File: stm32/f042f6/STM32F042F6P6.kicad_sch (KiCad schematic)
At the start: 29 parts, among them J1 STLINK, J3 L, J3 USB_C_REC_16PIN, J4 R, SW1 BOOT0, U1 XC6220B331MR, U2 STM32F042F6Px, Y1 8 MHz

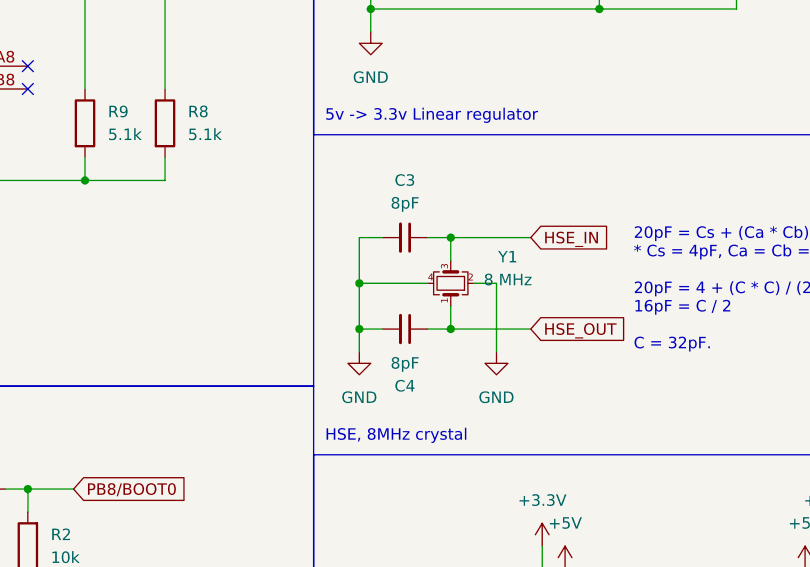
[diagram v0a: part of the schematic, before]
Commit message: Update README.md and mistyped capacitor size correction.
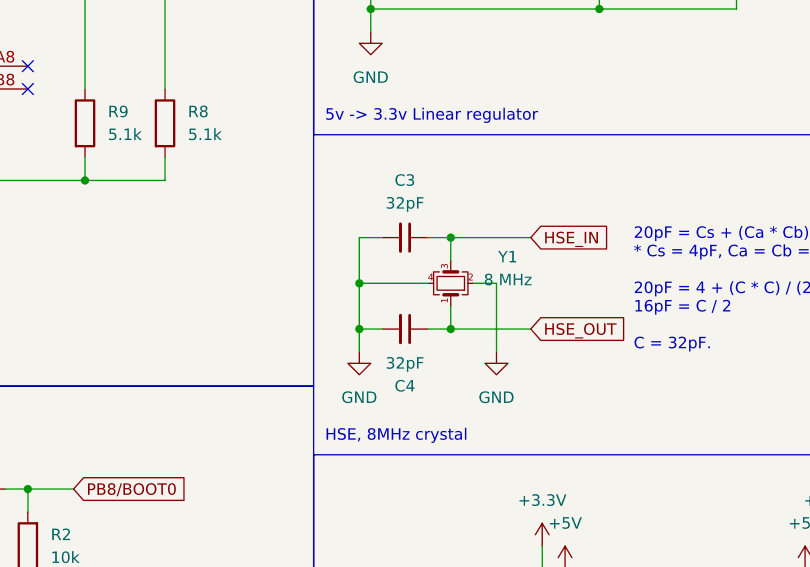
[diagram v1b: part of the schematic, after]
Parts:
- C3, C4: value 8pF -> 32pF
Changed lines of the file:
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@@
       (effects (font (size 1.27 1.27)))
     )
-    (property "Value" "8pF" (at 95.2436 77.47 90)
+    (property "Value" "32pF" (at 95.2436 77.47 90)
       (effects (font (size 1.27 1.27)))
     )
@@
       (effects (font (size 1.27 1.27)))
     )
-    (property "Value" "8pF" (at 95.2436 95.25 90)
-      (effects (font (size 1.27 1.27)))
-    )
+    (property "Value" "32pF" (at 95.2436 95.25 90)
+      (effects (font (size 1.27 1.27)))
+    )

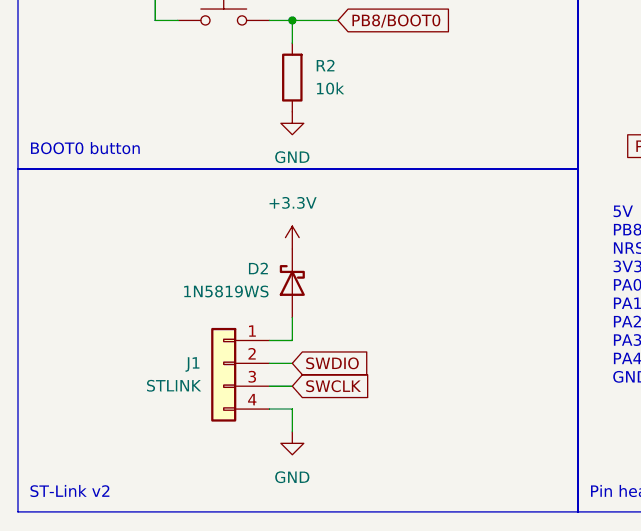
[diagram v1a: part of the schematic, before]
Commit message: WIP: F070F6P6, Fix: Diode direction corrected for F042F6P6.
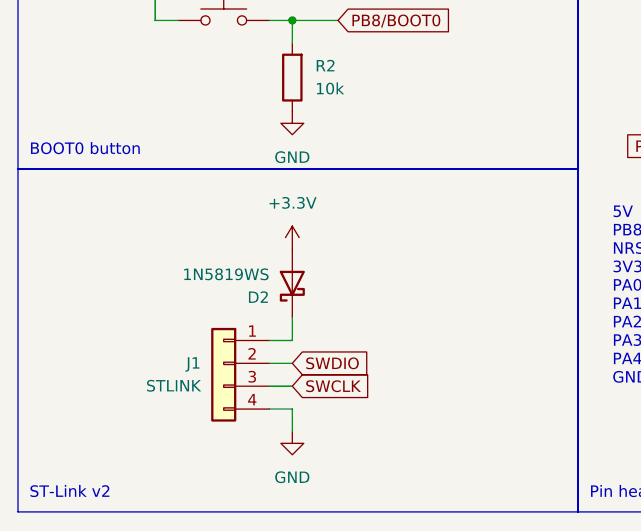
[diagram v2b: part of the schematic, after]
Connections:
- net +3.3V: now also D2.2 (A); no longer D2.1 (K)
- net at J1.1 (Pin_1): now also D2.1 (K); no longer D2.2 (A)
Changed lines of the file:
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@@
     )
   )
-  (symbol (lib_id "Diode:1N5819WS") (at 53.34 138.43 90) (mirror x) (unit 1)
+  (symbol (lib_id "Diode:1N5819WS") (at 53.34 138.43 90) (unit 1)
     (in_bom yes) (on_board yes) (dnp no)
-    (property "Reference" "D2" (at 50.8 136.8425 90)
+    (property "Reference" "D2" (at 50.8 140.0175 90)
       (effects (font (size 1.27 1.27)) (justify left))
     )
-    (property "Value" "1N5819WS" (at 50.8 139.3825 90)
+    (property "Value" "1N5819WS" (at 50.8 137.4775 90)
       (effects (font (size 1.27 1.27)) (justify left))
     )

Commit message: Fix: Diode direction corrected.
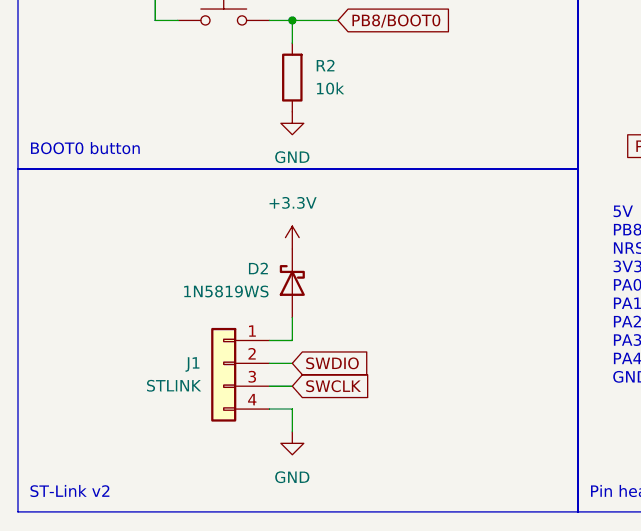
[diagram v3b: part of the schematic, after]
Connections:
- net +3.3V: now also D2.1 (K); no longer D2.2 (A)
- net at J1.1 (Pin_1): now also D2.2 (A); no longer D2.1 (K)
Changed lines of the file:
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@@
     )
   )
-  (symbol (lib_id "Diode:1N5819WS") (at 53.34 138.43 90) (unit 1)
+  (symbol (lib_id "Diode:1N5819WS") (at 53.34 138.43 90) (mirror x) (unit 1)
     (in_bom yes) (on_board yes) (dnp no)
-    (property "Reference" "D2" (at 50.8 140.0175 90)
+    (property "Reference" "D2" (at 50.8 136.8425 90)
       (effects (font (size 1.27 1.27)) (justify left))
     )
-    (property "Value" "1N5819WS" (at 50.8 137.4775 90)
+    (property "Value" "1N5819WS" (at 50.8 139.3825 90)
       (effects (font (size 1.27 1.27)) (justify left))
     )

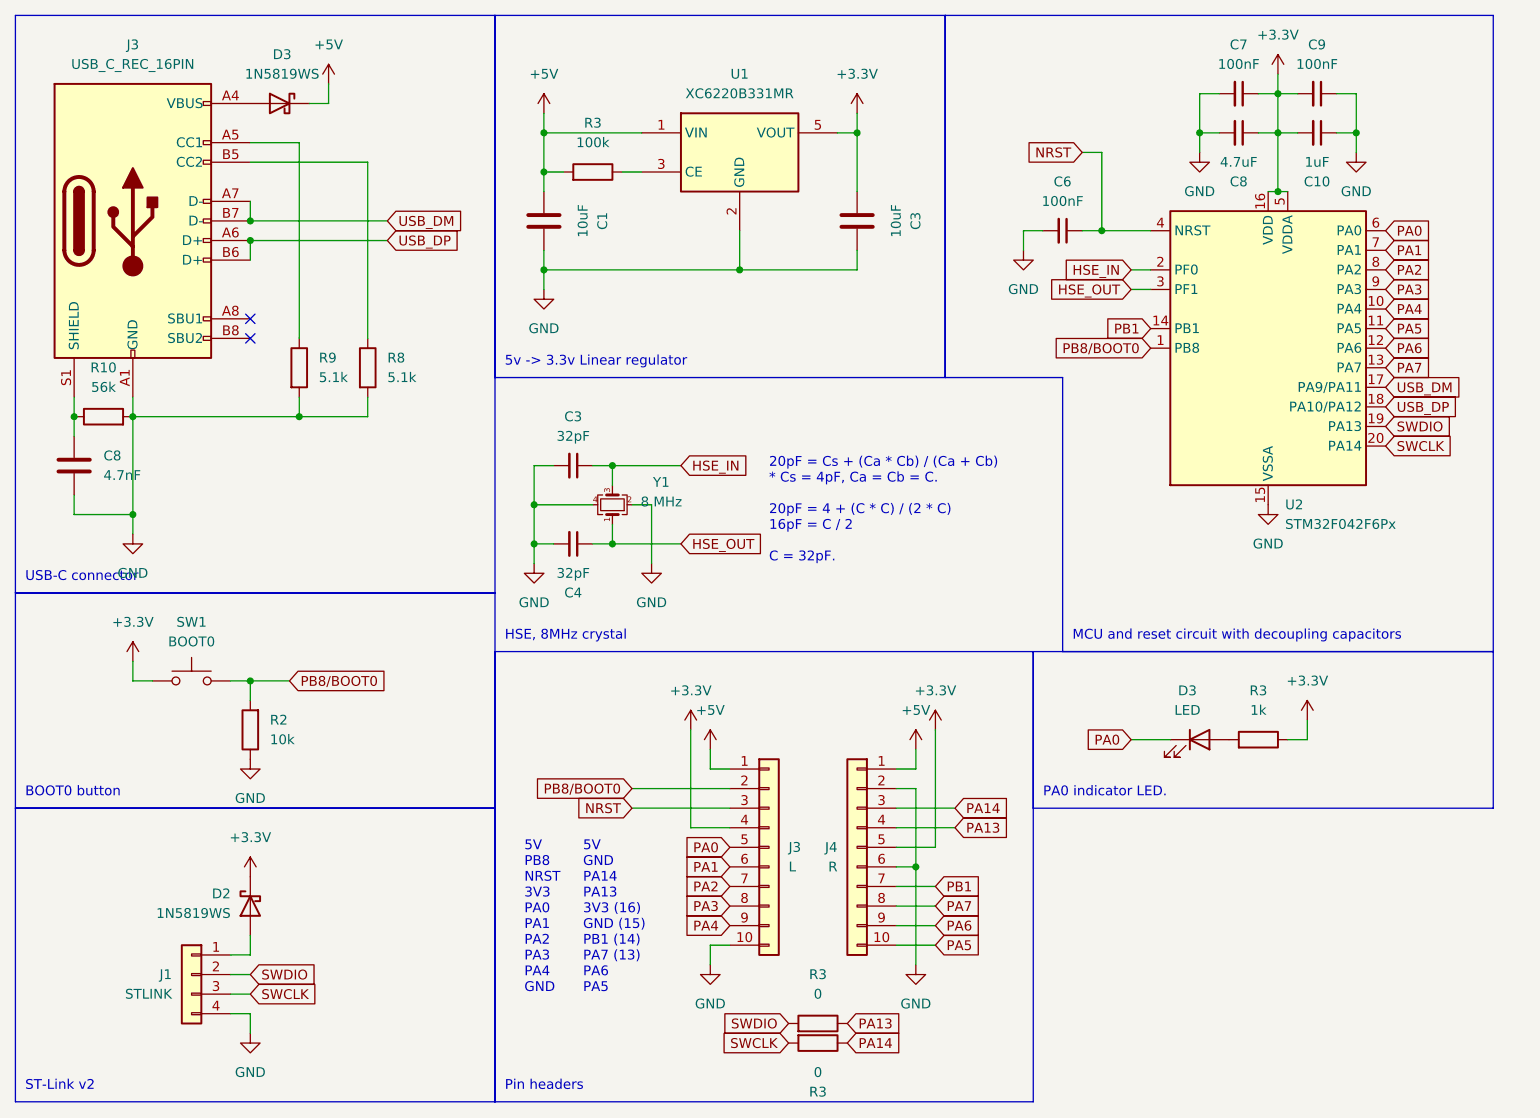
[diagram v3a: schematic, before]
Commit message: F042: HSE crystal removal because it didn't be needed.
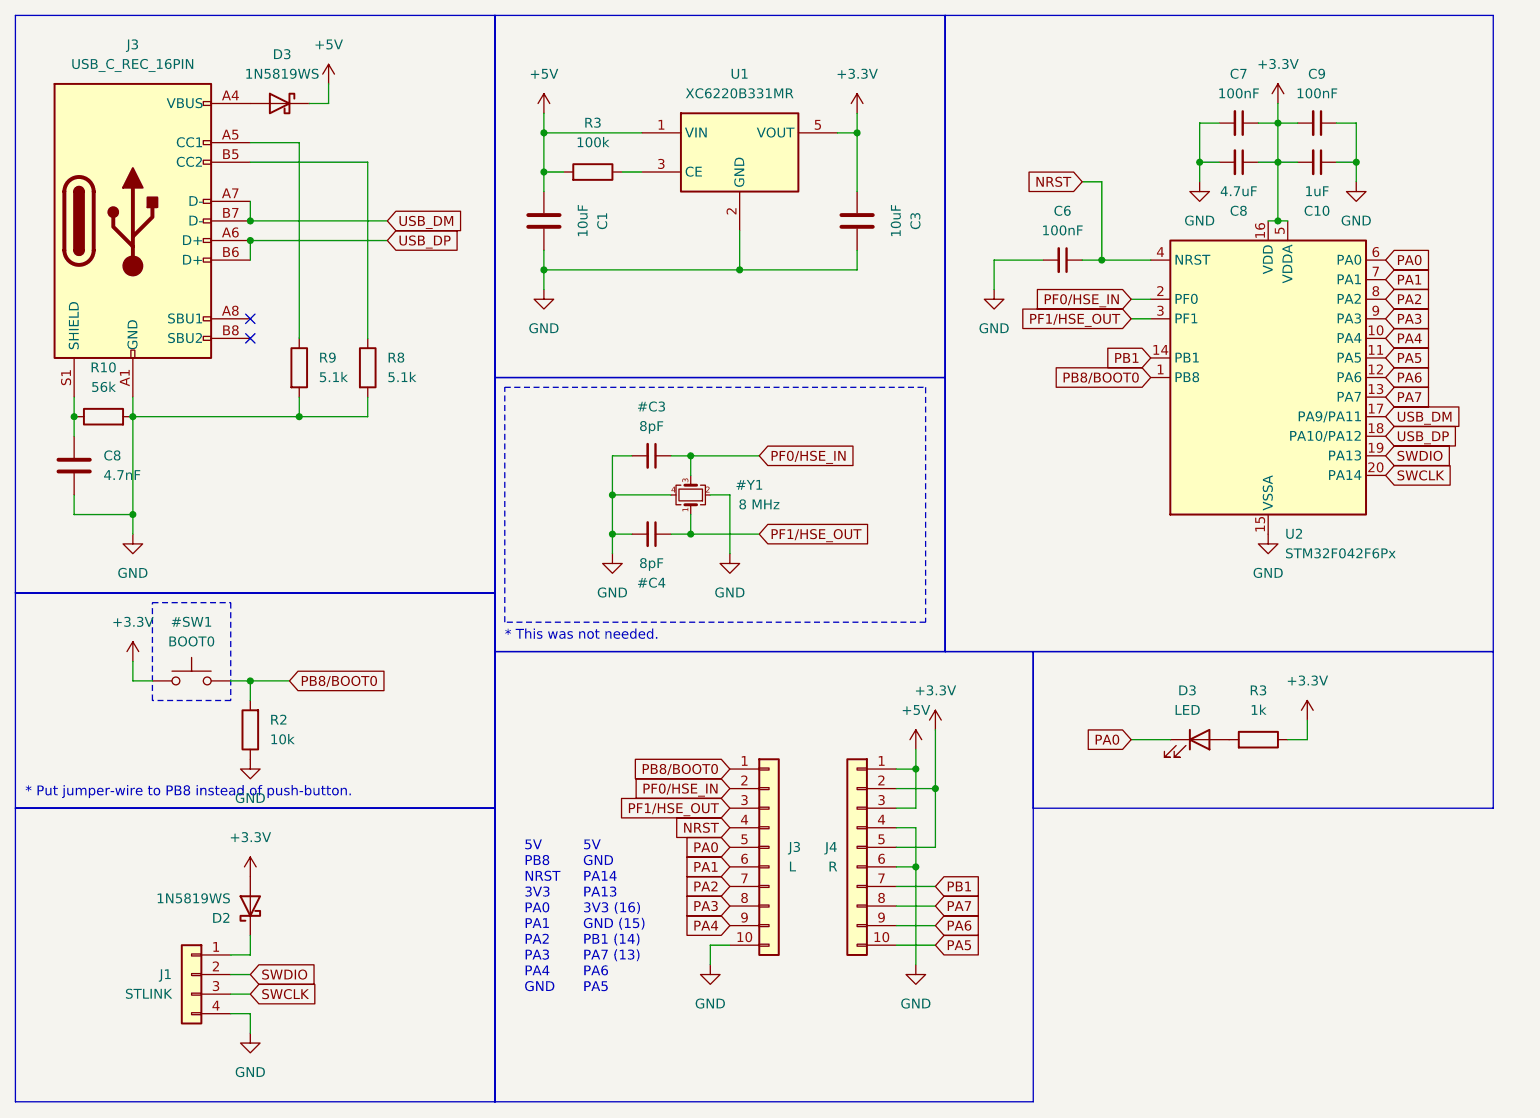
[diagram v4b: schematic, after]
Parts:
- removed R3 (x2): 0, Resistor_SMD:R_0603_1608Metric, symbol Device:R
- #C3: renamed from C3; value 32pF -> 8pF
- #C4: renamed from C4; value 32pF -> 8pF
- renumbered SW1 to #SW1, Y1 to #Y1
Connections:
- net PA13 is gone; now on net GND: J4.4 (Pin_4)
- net PA14 is gone; now on net +5V: J4.3 (Pin_3)
- net +3.3V: now also D2.2 (A), J4.2 (Pin_2); no longer D2.1 (K), J3.4 (Pin_4)
- net +5V: no longer J3.1 (Pin_1)
- net GND: no longer J4.2 (Pin_2)
- net NRST: now also J3.4 (Pin_4); no longer J3.3 (Pin_3)
- net PB8/BOOT0: now also J3.1 (Pin_1); no longer J3.2 (Pin_2)
- net at J1.1 (Pin_1): now also D2.1 (K); no longer D2.2 (A)
- net HSE_IN renamed PF0/HSE_IN
- net PF0/HSE_IN: now also J3.2 (Pin_2)
- net HSE_OUT renamed PF1/HSE_OUT
- net PF1/HSE_OUT: now also J3.3 (Pin_3)
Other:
- note added: "* Put jumper-wire to PB8 instead of push-button."
- note added: "* This was not needed."
- note removed: "20pF = Cs + (Ca * Cb) / (Ca + Cb) * Cs = 4pF, Ca = Cb = C. 20pF = 4 + (C * C) / (2 * C) 16pF = C / 2 C = 32pF."
- note removed: "5v -> 3.3v Linear regulator"
- note removed: "BOOT0 button"
- note removed: "HSE, 8MHz crystal"
- note removed: "MCU and reset circuit with decoupling capacitors"
- note removed: "PA0 indicator LED."
- note removed: "Pin headers"
- note removed: "ST-Link v2"
- note removed: "USB-C connector"
- moved on the sheet: C10, C6, C7, C8, C9, U2

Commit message: `F042` board completed
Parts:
- #C3, #C4: value 8pF -> 30pF
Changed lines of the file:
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@@
       (effects (font (size 1.27 1.27)))
     )
-    (property "Value" "8pF" (at 105.4036 76.2 90)
+    (property "Value" "30pF" (at 105.4036 76.2 90)
       (effects (font (size 1.27 1.27)))
     )
@@
       (effects (font (size 1.27 1.27)))
     )
-    (property "Value" "8pF" (at 105.4036 93.98 90)
-      (effects (font (size 1.27 1.27)))
-    )
+    (property "Value" "30pF" (at 105.4036 93.98 90)
+      (effects (font (size 1.27 1.27)))
+    )
